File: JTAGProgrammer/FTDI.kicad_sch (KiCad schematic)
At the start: 29 parts, among them U1 FT2232HL, U3 93LC56B, Y1 RH100-12.000-10-3030-TR

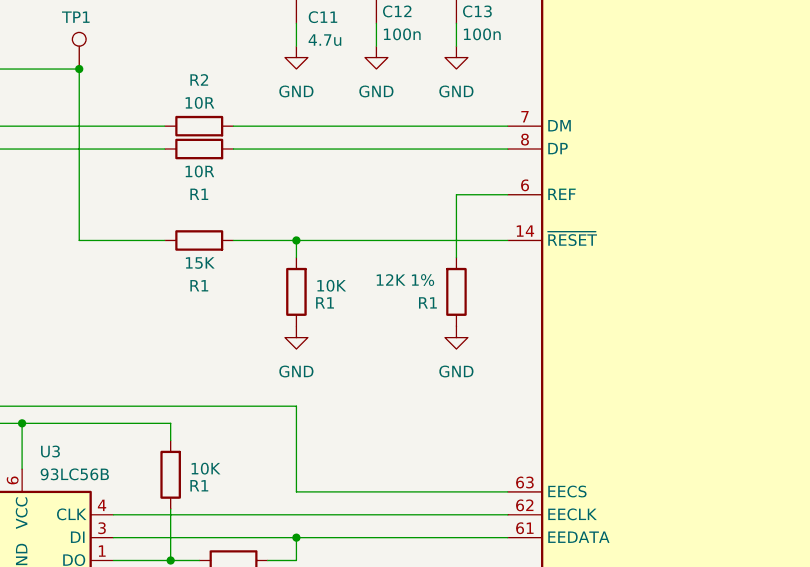
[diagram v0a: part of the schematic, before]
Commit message: Add LCSC part numbers
Signed-off-by: Anthony Bernaert <anthony.bernaert@gmail.com>
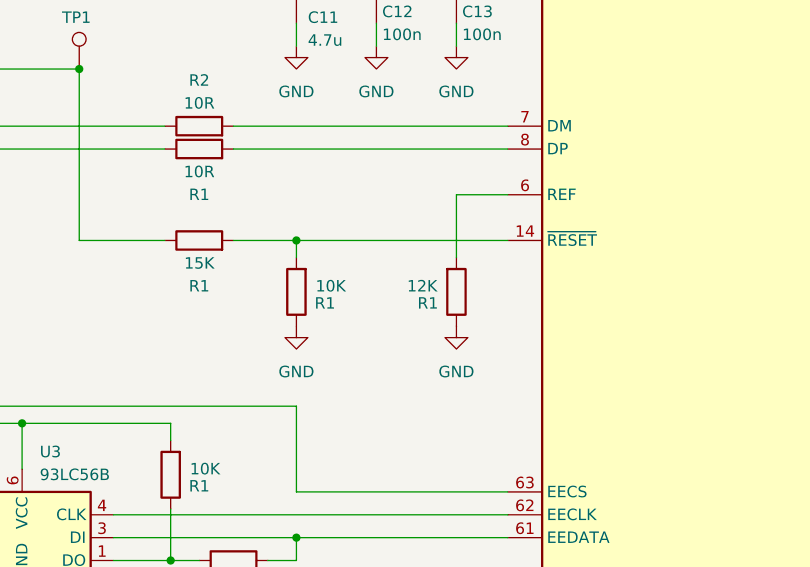
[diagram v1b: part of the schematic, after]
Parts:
- D1, D2: LCSC (none) -> C142698
- R1: value 12K 1% -> 12K
- U1: LCSC (none) -> C27882
- U3: LCSC (none) -> C190271
- Y1: LCSC (none) -> C255903
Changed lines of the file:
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@@
       (effects (font (size 1.27 1.27)) (justify bottom) hide)
+    )
+    (property "LCSC" "C142698" (at 50.165 84.455 90)
+      (effects (font (size 1.27 1.27)) hide)
     )
     (pin "1")
@@
       (effects (font (size 1.27 1.27)))
     )
-    (property "Value" "12K 1%" (at 123.825 89.535 0)
+    (property "Value" "12K" (at 125.73 90.17 0)
       (effects (font (size 1.27 1.27)))
     )
@@
       (effects (font (size 1.27 1.27)) (justify bottom) hide)
     )
+    (property "LCSC" "C142698" (at 54.61 84.455 90)
+      (effects (font (size 1.27 1.27)) hide)
+    )
     (pin "1")
     (pin "2")
@@
     )
     (property "Datasheet" "https://www.ftdichip.com/Support/Documents/DataSheets/ICs/DS_FT2232H.pdf" (at 165.735 95.25 0)
+      (effects (font (size 1.27 1.27)) hide)
+    )
+    (property "LCSC" "C27882" (at 165.735 95.25 0)
       (effects (font (size 1.27 1.27)) hide)
     )
@@
       (effects (font (size 1.27 1.27)) hide)
     )
+    (property "LCSC" "C255903" (at 108.585 146.685 0)
+      (effects (font (size 1.27 1.27)) hide)
+    )
     (pin "1")
     (pin "2")
@@
       (effects (font (size 1.27 1.27)) hide)
     )
+    (property "LCSC" "C190271" (at 81.28 118.11 0)
+      (effects (font (size 1.27 1.27)) hide)
+    )

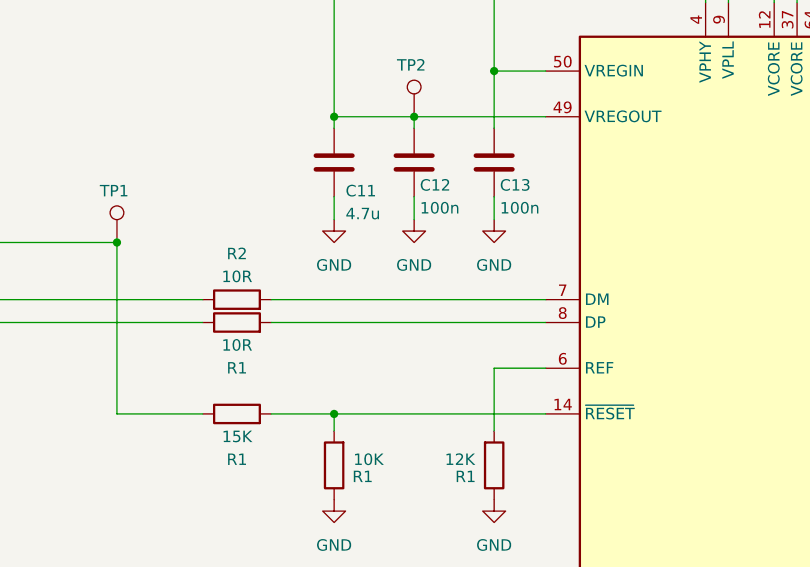
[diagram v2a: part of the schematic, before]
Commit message: Rev.2: change to USB Type-C, add VBUS fuse, VREF LED indicators
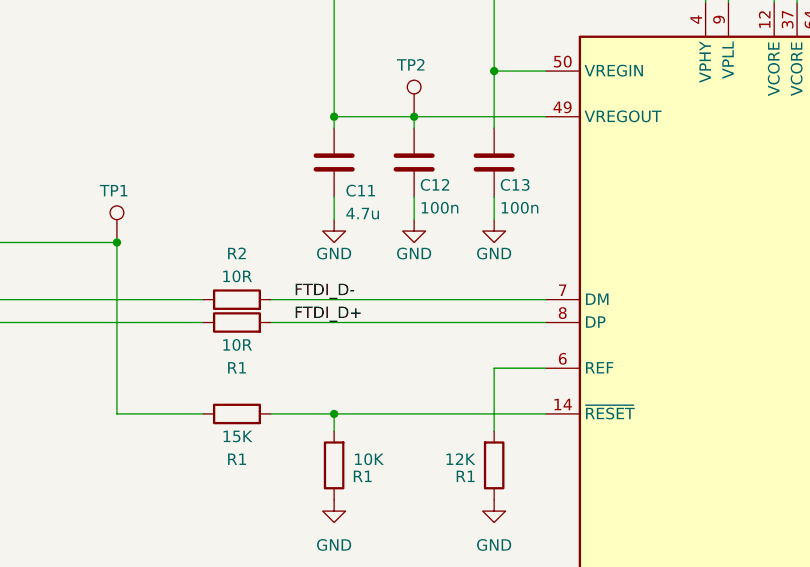
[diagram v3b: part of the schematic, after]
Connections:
- net FTDI_D+: now reaches R1.2, U1.8 (DP)
- net FTDI_D-: now reaches R2.2, U1.7 (DM)
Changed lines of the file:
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@@
     (title "FTDI JTAG Programmer")
     (date "2024-10-11")
-    (rev "1.1")
+    (rev "2")
   )
   (junction (at 111.76 118.11) (diameter 0) (color 0 0 0 0)
@@
     (stroke (width 0) (type default))
   )
+  (wire (pts (xy 63.5 127) (xy 81.28 127))
+    (stroke (width 0) (type default))
+  )
+  (wire (pts (xy 160.655 35.56) (xy 163.195 35.56))
+    (stroke (width 0) (type default))
+  )
+  (wire (pts (xy 155.575 33.02) (xy 155.575 39.37))
+    (stroke (width 0) (type default))
+  )
+  (wire (pts (xy 150.495 151.13) (xy 150.495 153.67))
+    (stroke (width 0) (type default))
+  )
+  (wire (pts (xy 111.76 120.65) (xy 108.585 120.65))
+    (stroke (width 0) (type default))
+  )
+  (wire (pts (xy 158.115 153.67) (xy 160.655 153.67))
+    (stroke (width 0) (type default))
+  )
+  (wire (pts (xy 229.235 132.715) (xy 229.235 138.43))
+    (stroke (width 0) (type default))
+  )
+  (wire (pts (xy 213.36 138.43) (xy 217.805 138.43))
+    (stroke (width 0) (type default))
+  )
+  (wire (pts (xy 111.76 29.21) (xy 111.76 52.07))
+    (stroke (width 0) (type default))
+  )
+  (wire (pts (xy 196.215 54.61) (xy 216.535 54.61))
+    (stroke (width 0) (type default))
+  )
+  (wire (pts (xy 116.205 125.73) (xy 135.255 125.73))
+    (stroke (width 0) (type default))
+  )
+  (wire (pts (xy 97.79 105.41) (xy 97.79 107.315))
+    (stroke (width 0) (type default))
+  )
+  (wire (pts (xy 170.815 39.37) (xy 170.815 35.56))
+    (stroke (width 0) (type default))
+  )
+  (wire (pts (xy 92.71 146.685) (xy 92.71 133.35))
+    (stroke (width 0) (type default))
+  )
+  (wire (pts (xy 69.85 177.8) (xy 69.85 181.61))
+    (stroke (width 0) (type default))
+  )
+  (wire (pts (xy 92.71 133.35) (xy 116.205 133.35))
+    (stroke (width 0) (type default))
+  )
+  (wire (pts (xy 170.815 153.67) (xy 173.355 153.67))
+    (stroke (width 0) (type default))
+  )
+  (wire (pts (xy 97.79 114.935) (xy 97.79 120.65))
+    (stroke (width 0) (type default))
+  )
   (wire (pts (xy 104.775 72.39) (xy 135.255 72.39))
     (stroke (width 0) (type default))
   )
-  (wire (pts (xy 63.5 127) (xy 81.28 127))
-    (stroke (width 0) (type default))
-  )
-  (wire (pts (xy 160.655 35.56) (xy 163.195 35.56))
-    (stroke (width 0) (type default))
-  )
-  (wire (pts (xy 155.575 33.02) (xy 155.575 39.37))
-    (stroke (width 0) (type default))
-  )
-  (wire (pts (xy 150.495 151.13) (xy 150.495 153.67))
-    (stroke (width 0) (type default))
-  )
-  (wire (pts (xy 111.76 120.65) (xy 108.585 120.65))
-    (stroke (width 0) (type default))
-  )
-  (wire (pts (xy 158.115 153.67) (xy 160.655 153.67))
-    (stroke (width 0) (type default))
-  )
-  (wire (pts (xy 229.235 132.715) (xy 229.235 138.43))
-    (stroke (width 0) (type default))
-  )
-  (wire (pts (xy 213.36 138.43) (xy 217.805 138.43))
-    (stroke (width 0) (type default))
-  )
-  (wire (pts (xy 111.76 29.21) (xy 111.76 52.07))
-    (stroke (width 0) (type default))
-  )
-  (wire (pts (xy 196.215 54.61) (xy 216.535 54.61))
-    (stroke (width 0) (type default))
-  )
-  (wire (pts (xy 116.205 125.73) (xy 135.255 125.73))
-    (stroke (width 0) (type default))
-  )
-  (wire (pts (xy 97.79 105.41) (xy 97.79 107.315))
-    (stroke (width 0) (type default))
-  )
-  (wire (pts (xy 170.815 39.37) (xy 170.815 35.56))
-    (stroke (width 0) (type default))
-  )
-  (wire (pts (xy 92.71 146.685) (xy 92.71 133.35))
-    (stroke (width 0) (type default))
-  )
-  (wire (pts (xy 69.85 177.8) (xy 69.85 181.61))
-    (stroke (width 0) (type default))
-  )
-  (wire (pts (xy 92.71 133.35) (xy 116.205 133.35))
-    (stroke (width 0) (type default))
-  )
-  (wire (pts (xy 170.815 153.67) (xy 173.355 153.67))
-    (stroke (width 0) (type default))
-  )
-  (wire (pts (xy 97.79 114.935) (xy 97.79 120.65))
-    (stroke (width 0) (type default))
-  )
   (wire (pts (xy 111.76 103.505) (xy 111.76 113.03))
     (stroke (width 0) (type default))
@@
   (wire (pts (xy 81.28 127) (xy 81.28 125.73))
     (stroke (width 0) (type default))
+  )
+  (label "FTDI_D-" (at 107.315 72.39 0) (fields_autoplaced)
+    (effects (font (size 1.27 1.27)) (justify left bottom))
+  )
+  (label "FTDI_D+" (at 107.315 74.93 0) (fields_autoplaced)
+    (effects (font (size 1.27 1.27)) (justify left bottom))
   )
   (hierarchical_label "USB_DP" (shape input) (at 45.085 74.93 180) (fields_autoplaced)
@@
   (hierarchical_label "UART_RXD" (shape input) (at 216.535 95.25 0) (fields_autoplaced)
     (effects (font (size 1.27 1.27)) (justify left))
+  )
+  (netclass_flag "" (length 2.54) (shape round) (at 118.745 74.93 180) (fields_autoplaced)
+    (effects (font (size 1.27 1.27)) (justify right bottom))
+    (property "Netclass" "USB_DIFF_PAIR" (at 119.4435 77.47 0)
+      (effects (font (size 1.27 1.27) italic) (justify left))
+    )
+  )
+  (netclass_flag "" (length 2.54) (shape round) (at 118.745 72.39 0) (fields_autoplaced)
+    (effects (font (size 1.27 1.27)) (justify left bottom))
+    (property "Netclass" "USB_DIFF_PAIR" (at 119.4435 69.85 0)
+      (effects (font (size 1.27 1.27) italic) (justify left))
+    )
   )
   (symbol (lib_id "power:+3V3") (at 62.23 167.005 0) (unit 1)
@@
   )
   (symbol (lib_id "power:GND") (at 120.65 63.5 0) (unit 1)
-    (in_bom yes) (on_board yes) (dnp no) (fields_autoplaced)
+    (in_bom yes) (on_board yes) (dnp no)
     (property "Reference" "#PWR014" (at 120.65 69.85 0)
       (effects (font (size 1.27 1.27)) hide)
     )
-    (property "Value" "GND" (at 120.65 68.58 0)
+    (property "Value" "GND" (at 120.65 67.31 0)
       (effects (font (size 1.27 1.27)))
     )
@@
       (effects (font (size 1.27 1.27)) hide)
     )
-    (property "Value" "GND" (at 111.76 68.58 0)
+    (property "Value" "GND" (at 111.76 67.31 0)
       (effects (font (size 1.27 1.27)))
     )
@@
   )
   (symbol (lib_id "power:GND") (at 129.54 63.5 0) (unit 1)
-    (in_bom yes) (on_board yes) (dnp no) (fields_autoplaced)
+    (in_bom yes) (on_board yes) (dnp no)
     (property "Reference" "#PWR015" (at 129.54 69.85 0)
       (effects (font (size 1.27 1.27)) hide)
     )
-    (property "Value" "GND" (at 129.54 68.58 0)
-      (effects (font (size 1.27 1.27)))
-    )
+    (property "Value" "GND" (at 129.54 67.31 0)
+      (effects (font (size 1.27 1.27)))
+    )
